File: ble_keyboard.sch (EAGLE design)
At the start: 10 parts, among them CN1 FH34SRJ-6S, CN2 FH34SRJ-10S, CN3 3711-007549, CON1 41002W90-NP-S-30

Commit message: BRD routed
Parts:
- removed CN3: 3711-007549, 3711-007549:3711-007549
- removed R3, R4: 2K, rcl:R-EU_R0603
- added C1: 10nF, rcl:C-EUC0603
- added C2, C5, C7: 100n, rcl:C-EUC0603
- added C3, C6: 1uF, rcl:C-EUC0603
- added C4: 100nF, rcl:C-EUC0603
- added CIN_VIN: 53047-04, con-molex:53047-04
- added Q1: DMG6968U-7, SparkFun:MOSFET-NCHANNELSMD
- added RN1: 2K, dp_devices:RESISTOR_ARRAY_4
- added VREG1: MIC5200-3.3YS, dp_devices:VREG_3PINS-SOT-223
- R1: value 2K -> 47K
- R2: value 2K -> 10
- U1: value (none) -> YJ-14015
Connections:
- removed net BACKL_LED_A: CN1.1, CN1.2
- removed net BAT_DETECT: CN3.6
- removed net VBAT: CN3.1, CN3.2, CN3.3
- removed net VBAT_ADC: U1.P0.01
- new net LIPO_RAW: CIN_VIN-1.S, CN1.1, CN1.2, VREG1.VIN
- new net MOTOR_A_GATE_R: Q1.G, R1.1, R2.2
- net +3V3: now also C1.1, C2.1, C3.1, C4.1, C5.1, C6.1, C7.1, VREG1.VOUT
- net BACKLIGHT_PWM: now also R2.1
- net BACKL_LED_K: now also Q1.D
- net GND: now also C1.2, C2.2, C3.2, C4.2, C5.2, C6.2, C7.2, CIN_VIN-4.S, Q1.S, R1.2, VREG1.GND; no longer CN3.7, CN3.8, CN3.9, CN3.MH1, CN3.MH2
- net I2C_SCL: now also CIN_VIN-3.S; no longer CN3.4
- net I2C_SDA: now also CIN_VIN-2.S; no longer CN3.5
- net KSI0: now also U1.P0.25; no longer U1.P0.21
- net KSI1: now also U1.P0.27; no longer U1.P0.22
- net KSI2: now also U1.P0.28; no longer U1.P0.23
- net KSI3: now also U1.P0.29; no longer U1.P0.24
- net KSI4: now also U1.P0.30; no longer U1.P0.25
- net KSI5: now also U1.P0.02; no longer U1.P0.26
- net KSI6: now also U1.P0.04; no longer U1.P0.27
- net KSI7: now also U1.P0.05; no longer U1.P0.28
- net KSO0: now also U1.P0.21; no longer U1.P0.00
- net KSO1: now also U1.P0.22; no longer U1.P0.30
- net KSO10: now also U1.P0.09; no longer U1.P0.10
- net KSO11: now also U1.P0.10; no longer U1.P0.11
- net KSO12: now also U1.P0.11; no longer U1.P0.12
- net KSO13: now also U1.P0.12; no longer U1.P0.13
- net KSO14: now also U1.P0.13; no longer U1.P0.14
- net KSO15: now also U1.P0.14; no longer U1.P0.15
- net KSO2: now also U1.P0.23; no longer U1.P0.02
- net KSO3: now also U1.P0.24; no longer U1.P0.03
- net KSO4: now also U1.P0.26; no longer U1.P0.04
- net KSO5: now also U1.P0.00; no longer U1.P0.05
- net KSO6: now also U1.P0.03; no longer U1.P0.06
- net KSO7: now also U1.P0.06; no longer U1.P0.07
- net KSO8: now also U1.P0.07; no longer U1.P0.08
- net KSO9: now also U1.P0.08; no longer U1.P0.09
- net LED_CAPS: now also RN1B.1, U1.P0.15; no longer R3.1, U1.P0.19
- net LED_FN: now also RN1A.1, U1.P0.19; no longer R4.1, U1.P0.29
- net LED_RFOFF: now also RN1C.1; no longer R2.1
- net LED_TP: now also RN1D.1; no longer R1.1
- net N$1: now also RN1D.2; no longer R1.2
- net N$2: now also RN1C.2; no longer R2.2
- net N$3: now also RN1B.2; no longer R3.2
- net N$4: now also RN1A.2; no longer R4.2
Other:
- note added: "+3V3 decoupling"
- note added: "KBD backlight driver"
- note added: "Power input & gauge SMBUS"
- note removed: "Battery connector"
- moved on the sheet: R1, R2

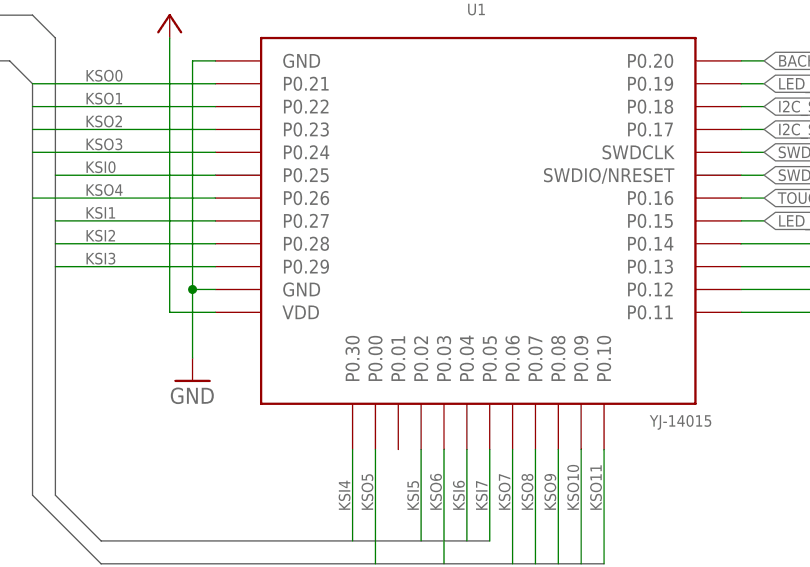
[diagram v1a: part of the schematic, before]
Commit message: - Save before BLE module rotation. - Added note abotu the best antenna gain.
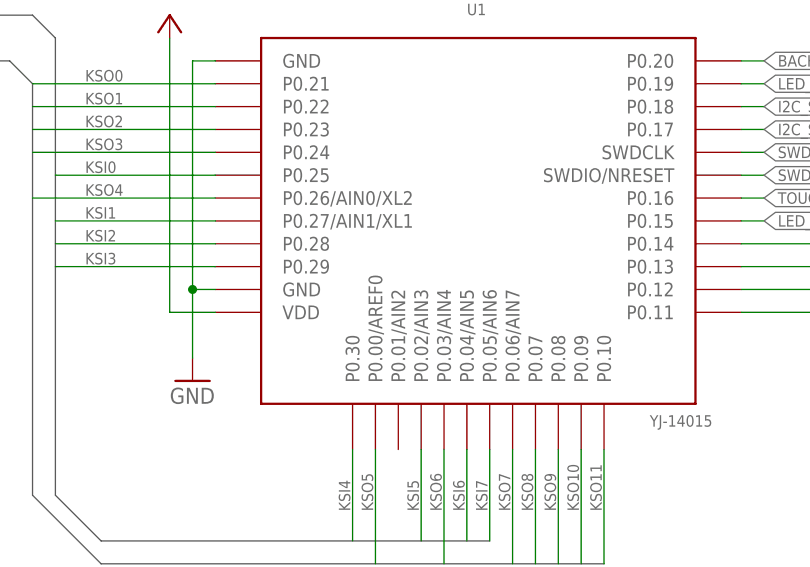
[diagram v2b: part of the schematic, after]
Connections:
- net KSI1: now also U1.P0.27/AIN1/XL1; no longer U1.P0.27
- net KSI5: now also U1.P0.02/AIN3; no longer U1.P0.02
- net KSI6: now also U1.P0.04/AIN5; no longer U1.P0.04
- net KSI7: now also U1.P0.05/AIN6; no longer U1.P0.05
- net KSO4: now also U1.P0.26/AIN0/XL2; no longer U1.P0.26
- net KSO5: now also U1.P0.00/AREF0; no longer U1.P0.00
- net KSO6: now also U1.P0.03/AIN4; no longer U1.P0.03
- net KSO7: now also U1.P0.06/AIN7; no longer U1.P0.06
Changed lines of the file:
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@@
 <wire x1="43.18" y1="76.2" x2="25.4" y2="76.2" width="0.1524" layer="91"/>
 <label x="28.702" y="76.454" size="1.27" layer="95" font="vector"/>
-<pinref part="U1" gate="YJ-14015" pin="P0.27"/>
+<pinref part="U1" gate="YJ-14015" pin="P0.27/AIN1/XL1"/>
 </segment>
 </net>
@@
 <wire x1="66.04" y1="50.8" x2="66.04" y2="40.64" width="0.1524" layer="91"/>
 <label x="65.786" y="43.942" size="1.27" layer="95" font="vector" rot="R90"/>
-<pinref part="U1" gate="YJ-14015" pin="P0.02"/>
+<pinref part="U1" gate="YJ-14015" pin="P0.02/AIN3"/>
 </segment>
 </net>
@@
 <wire x1="71.12" y1="50.8" x2="71.12" y2="40.64" width="0.1524" layer="91"/>
 <label x="70.866" y="43.942" size="1.27" layer="95" font="vector" rot="R90"/>
-<pinref part="U1" gate="YJ-14015" pin="P0.04"/>
+<pinref part="U1" gate="YJ-14015" pin="P0.04/AIN5"/>
 </segment>
 </net>
@@
 <wire x1="73.66" y1="50.8" x2="73.66" y2="40.64" width="0.1524" layer="91"/>
 <label x="73.406" y="43.942" size="1.27" layer="95" font="vector" rot="R90"/>
-<pinref part="U1" gate="YJ-14015" pin="P0.05"/>
+<pinref part="U1" gate="YJ-14015" pin="P0.05/AIN6"/>
 </segment>
 </net>
@@
 <wire x1="43.18" y1="78.74" x2="22.86" y2="78.74" width="0.1524" layer="91"/>
 <label x="28.702" y="78.994" size="1.27" layer="95" font="vector"/>
-<pinref part="U1" gate="YJ-14015" pin="P0.26"/>
+<pinref part="U1" gate="YJ-14015" pin="P0.26/AIN0/XL2"/>
 </segment>
 </net>
@@
 <wire x1="60.96" y1="50.8" x2="60.96" y2="38.1" width="0.1524" layer="91"/>
 <label x="60.706" y="43.942" size="1.27" layer="95" font="vector" rot="R90"/>
-<pinref part="U1" gate="YJ-14015" pin="P0.00"/>
+<pinref part="U1" gate="YJ-14015" pin="P0.00/AREF0"/>
 </segment>
 </net>
@@
 <wire x1="68.58" y1="50.8" x2="68.58" y2="38.1" width="0.1524" layer="91"/>
 <label x="68.326" y="43.942" size="1.27" layer="95" font="vector" rot="R90"/>
-<pinref part="U1" gate="YJ-14015" pin="P0.03"/>
+<pinref part="U1" gate="YJ-14015" pin="P0.03/AIN4"/>
 </segment>
 </net>
@@
 <wire x1="76.2" y1="50.8" x2="76.2" y2="38.1" width="0.1524" layer="91"/>
 <label x="75.946" y="43.942" size="1.27" layer="95" font="vector" rot="R90"/>
-<pinref part="U1" gate="YJ-14015" pin="P0.06"/>
+<pinref part="U1" gate="YJ-14015" pin="P0.06/AIN7"/>
 </segment>
 </net>

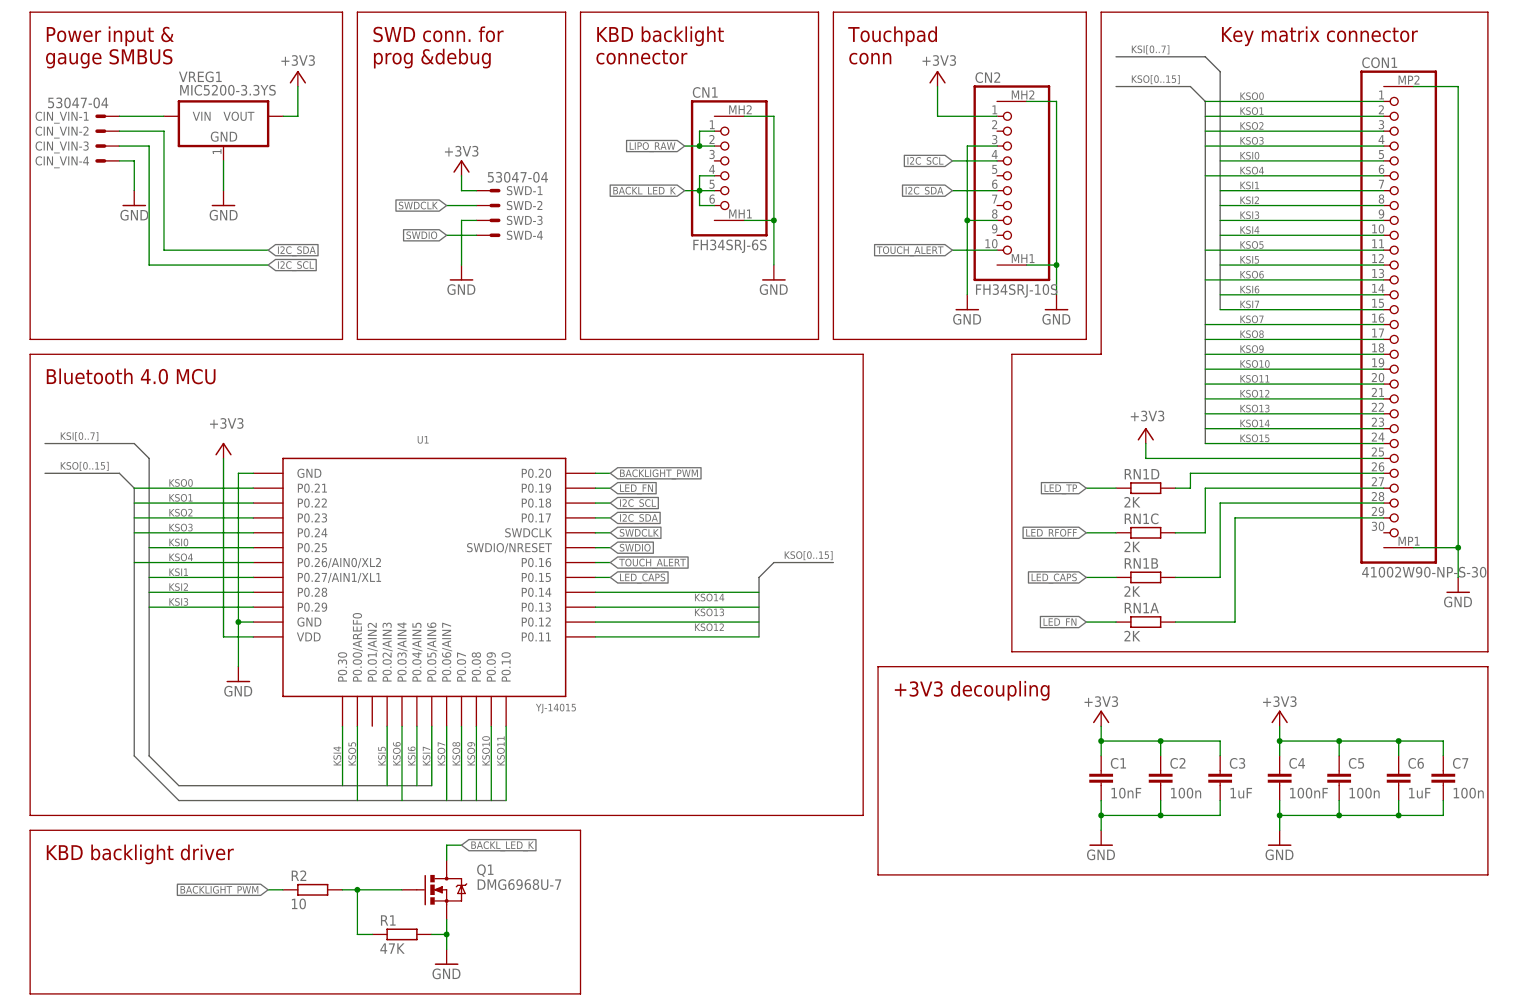
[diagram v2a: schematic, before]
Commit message: Brd routed with 90 degree rotated BLE module, fixed touchpad and Keyboard pinout
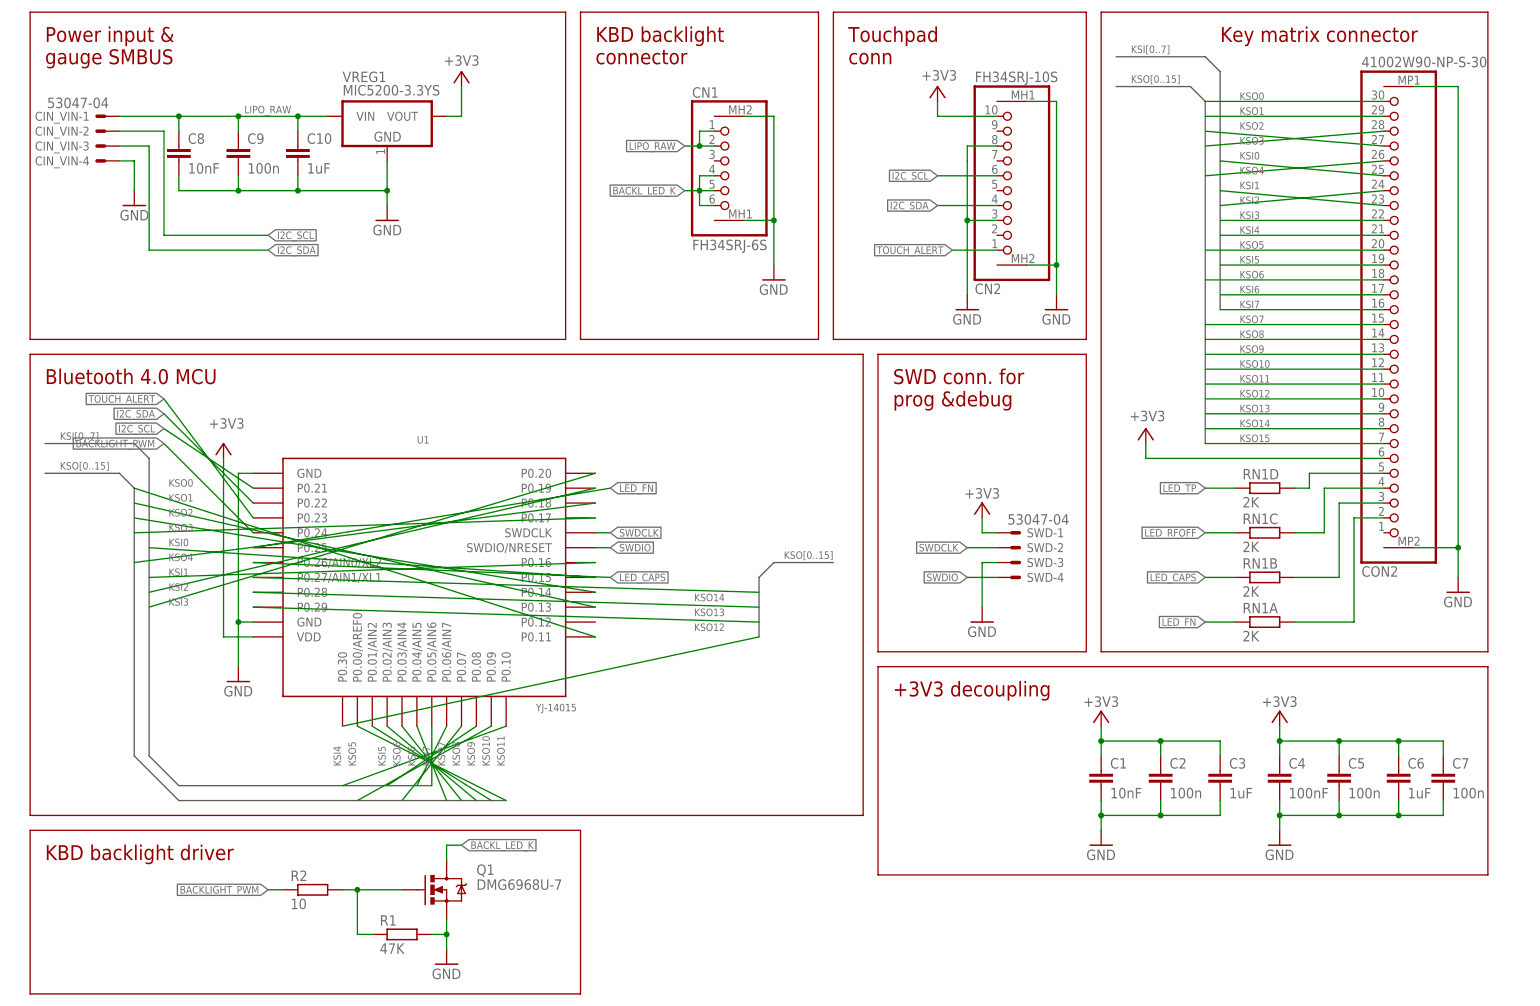
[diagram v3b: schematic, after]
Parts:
- removed CON1: 41002W90-NP-S-30, JTC41002:41002W90-NP-S-30
- added C10: 1uF, rcl:C-EUC0603
- added C8: 10nF, rcl:C-EUC0603
- added C9: 100n, rcl:C-EUC0603
- added CON2: 41002W90-NP-S-30, JTC41002:41002W90-NP-S-30
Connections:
- net +3V3: now also CN2.10, CON2.6; no longer CN2.1, CON1.25
- net BACKLIGHT_PWM: now also U1.P0.24; no longer U1.P0.20
- net GND: now also C10.2, C8.2, C9.2, CON2.MP1, CON2.MP2; no longer CON1.MP1, CON1.MP2
- net I2C_SCL: now also CIN_VIN-2.S, CN2.6, U1.P0.21; no longer CIN_VIN-3.S, CN2.4, U1.P0.18
- net I2C_SDA: now also CIN_VIN-3.S, CN2.4, U1.P0.22; no longer CIN_VIN-2.S, CN2.6, U1.P0.17
- net KSI0: now also CON2.25, U1.P0.15; no longer CON1.5, U1.P0.25
- net KSI1: now also CON2.23, U1.P0.16; no longer CON1.7, U1.P0.27/AIN1/XL1
- net KSI2: now also CON2.24, U1.P0.19; no longer CON1.8, U1.P0.28
- net KSI3: now also CON2.22, U1.P0.20; no longer CON1.9, U1.P0.29
- net KSI4: now also CON2.21, U1.P0.10; no longer CON1.10, U1.P0.30
- net KSI5: now also CON2.19, U1.P0.08; no longer CON1.12, U1.P0.02/AIN3
- net KSI6: now also CON2.17, U1.P0.06/AIN7; no longer CON1.14, U1.P0.04/AIN5
- net KSI7: now also CON2.16; no longer CON1.15
- net KSO0: now also CON2.30, U1.P0.11; no longer CON1.1, U1.P0.21
- net KSO1: now also CON2.29, U1.P0.13; no longer CON1.2, U1.P0.22
- net KSO10: now also CON2.12, U1.P0.01/AIN2; no longer CON1.19, U1.P0.09
- net KSO11: now also CON2.11, U1.P0.00/AREF0; no longer CON1.20, U1.P0.10
- net KSO12: now also CON2.10, U1.P0.30; no longer CON1.21, U1.P0.11
- net KSO13: now also CON2.9, U1.P0.29; no longer CON1.22, U1.P0.12
- net KSO14: now also CON2.8, U1.P0.28; no longer CON1.23, U1.P0.13
- net KSO15: now also CON2.7, U1.P0.27/AIN1/XL1; no longer CON1.24, U1.P0.14
- net KSO2: now also CON2.27, U1.P0.14; no longer CON1.3, U1.P0.23
- net KSO3: now also CON2.28, U1.P0.17; no longer CON1.4, U1.P0.24
- net KSO4: now also CON2.26, U1.P0.18; no longer CON1.6, U1.P0.26/AIN0/XL2
- net KSO5: now also CON2.20, U1.P0.09; no longer CON1.11, U1.P0.00/AREF0
- net KSO6: now also CON2.18, U1.P0.07; no longer CON1.13, U1.P0.03/AIN4
- net KSO7: now also CON2.15, U1.P0.04/AIN5; no longer CON1.16, U1.P0.06/AIN7
- net KSO8: now also CON2.14, U1.P0.03/AIN4; no longer CON1.17, U1.P0.07
- net KSO9: now also CON2.13, U1.P0.02/AIN3; no longer CON1.18, U1.P0.08
- net LED_CAPS: now also U1.P0.26/AIN0/XL2; no longer U1.P0.15
- net LED_FN: now also U1.P0.25; no longer U1.P0.19
- net LIPO_RAW: now also C10.1, C8.1, C9.1
- net N$1: now also CON2.5; no longer CON1.26
- net N$2: now also CON2.4; no longer CON1.27
- net N$3: now also CON2.3; no longer CON1.28
- net N$4: now also CON2.2; no longer CON1.29
- net TOUCH_ALERT: now also CN2.1, U1.P0.23; no longer CN2.10, U1.P0.16
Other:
- moved on the sheet: CN2, RN1A, RN1B, RN1C, RN1D, SWD-1, SWD-2, SWD-3, SWD-4, VREG1

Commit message: Cleaned up schematic mess, fixed keyboard BL pinout mirroring.
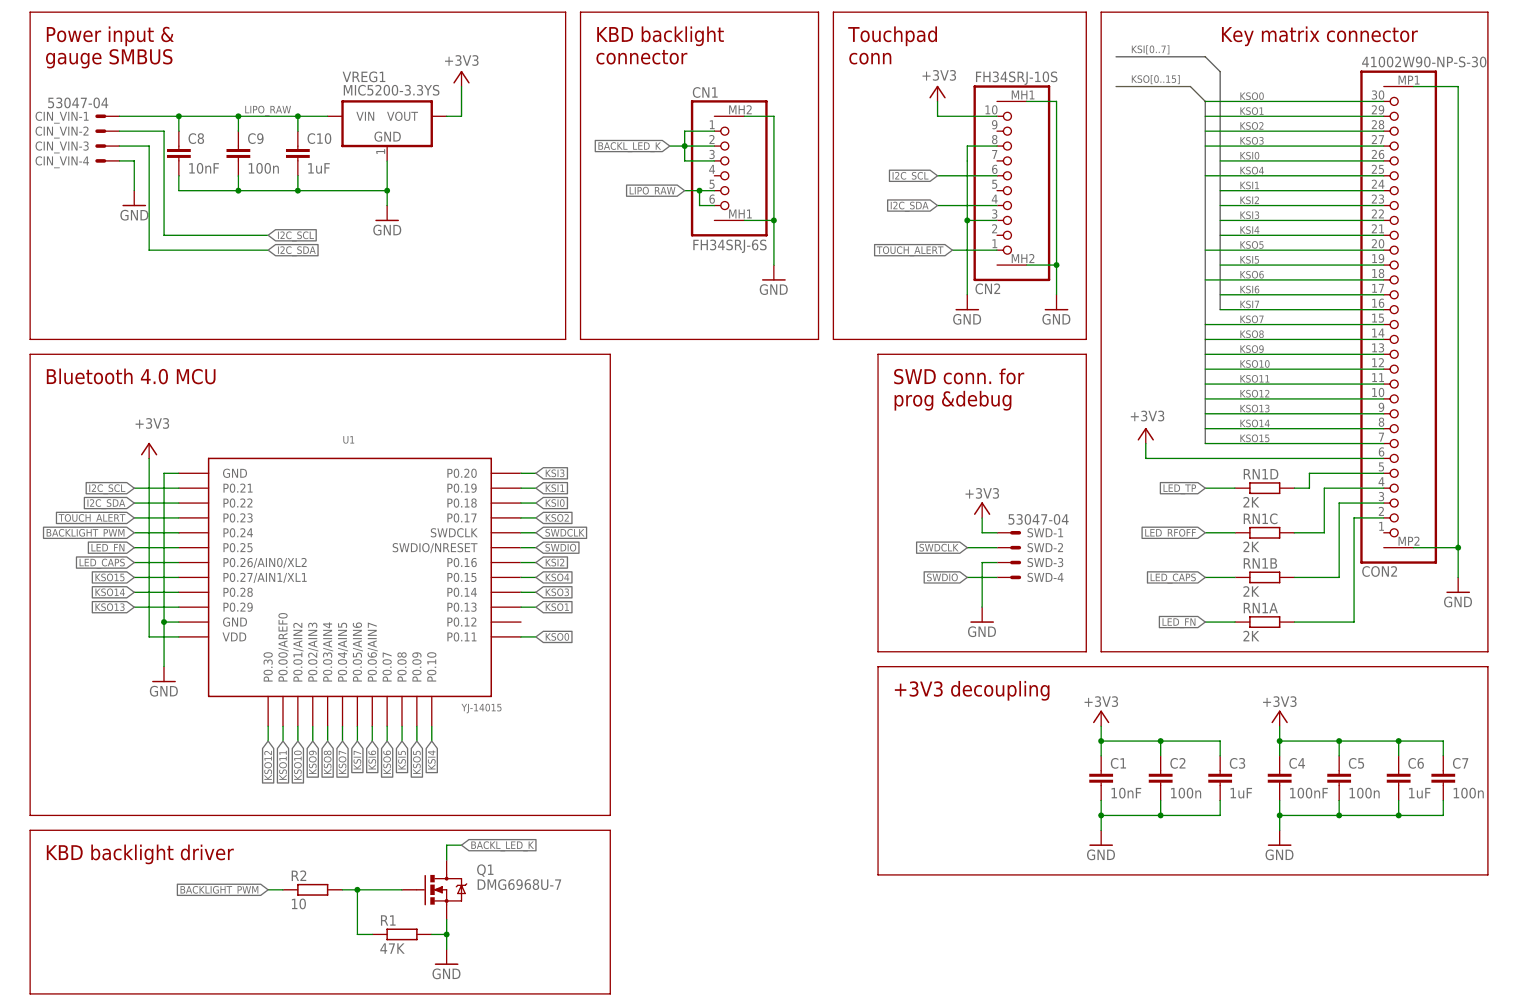
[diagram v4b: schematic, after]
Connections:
- net BACKL_LED_K: now also CN1.1, CN1.2, CN1.3; no longer CN1.4, CN1.5, CN1.6
- net KSI0: now also CON2.26, U1.P0.18; no longer CON2.25, U1.P0.15
- net KSI1: now also CON2.24, U1.P0.19; no longer CON2.23, U1.P0.16
- net KSI2: now also CON2.23, U1.P0.16; no longer CON2.24, U1.P0.19
- net KSO2: now also CON2.28, U1.P0.17; no longer CON2.27, U1.P0.14
- net KSO3: now also CON2.27, U1.P0.14; no longer CON2.28, U1.P0.17
- net KSO4: now also CON2.25, U1.P0.15; no longer CON2.26, U1.P0.18
- net LIPO_RAW: now also CN1.5, CN1.6; no longer CN1.1, CN1.2
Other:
- moved on the sheet: U1
